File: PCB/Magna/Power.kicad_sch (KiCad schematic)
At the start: 40 parts, among them U901 TPS61040DBV, U902 XL1509-ADJ, U903 WS3222D, U904 AMS1117-5.0, U905 AP2171W

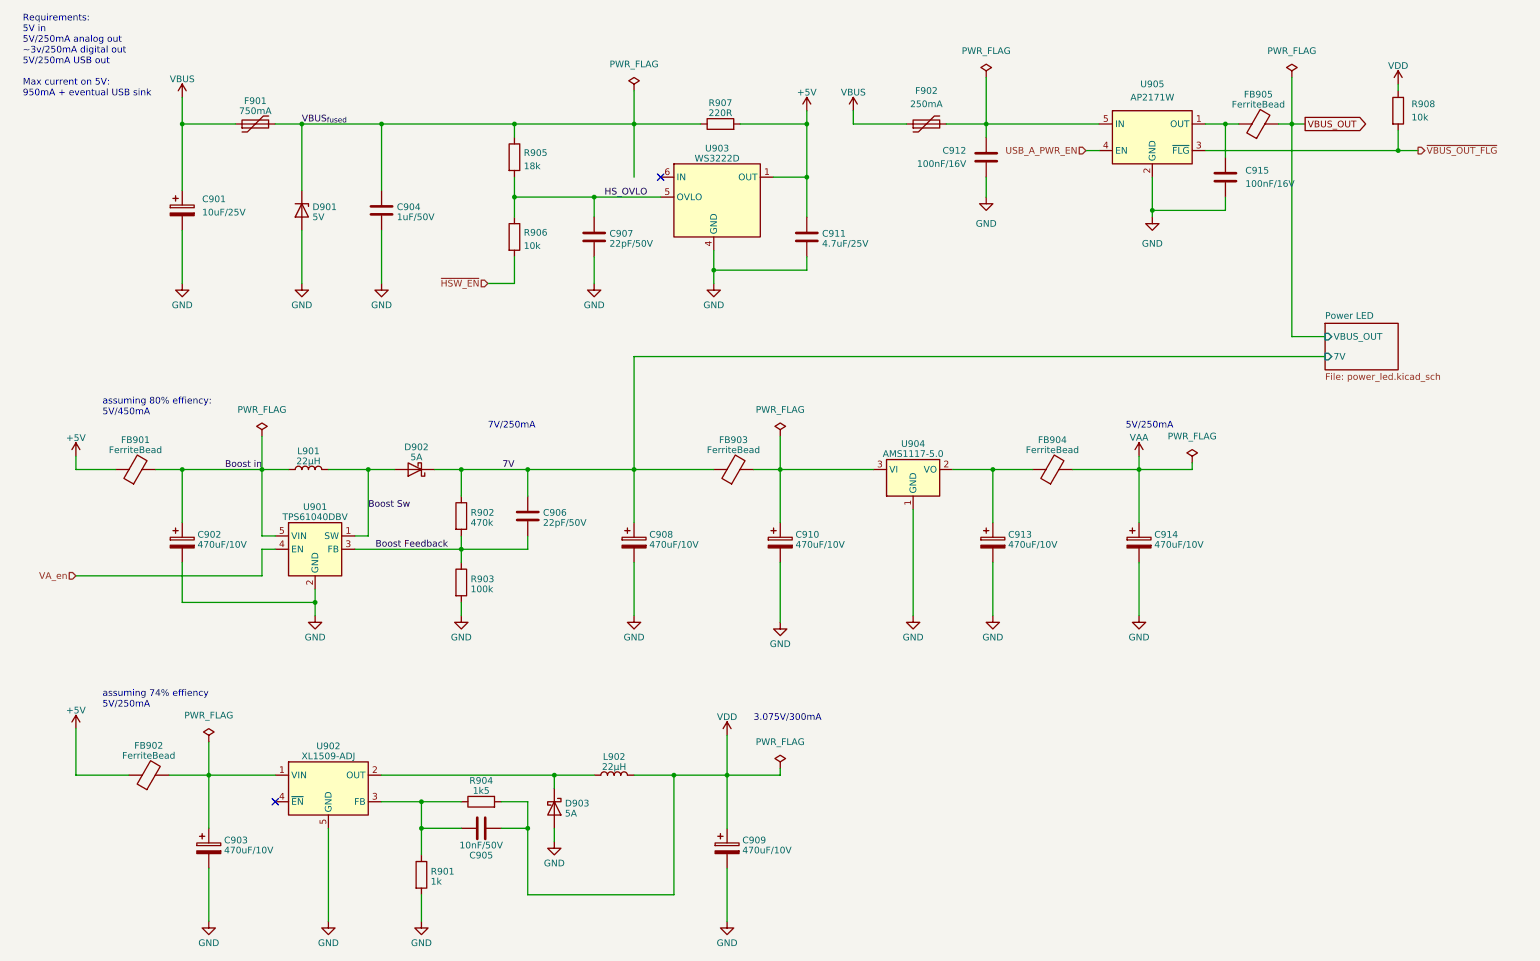
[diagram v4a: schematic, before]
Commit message: Select parts for all components
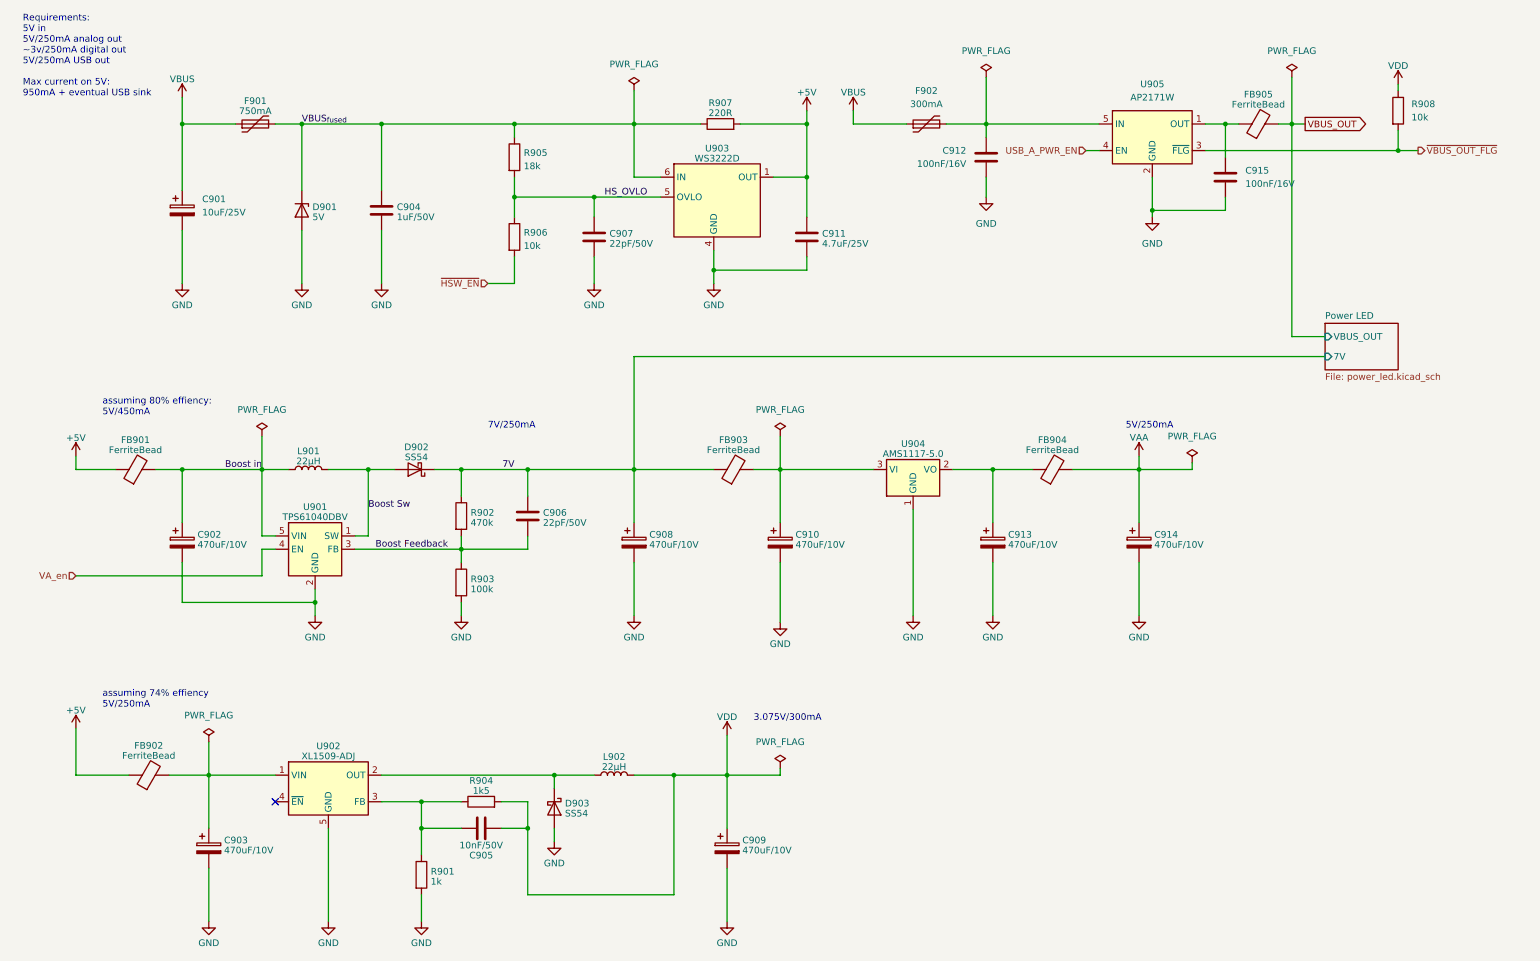
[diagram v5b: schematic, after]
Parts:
- D901: footprint Diode_SMD:D_SMC -> Diode_SMD:D_MELF_Handsoldering; LCSC (none) -> C8062
- D902, D903: value 5A -> SS54; footprint Diode_SMD:D_SMA -> Diode_SMD:D_SMA_Handsoldering; LCSC (none) -> C22452
- F901: footprint Fuse:Fuse_0805_2012Metric -> Fuse:Fuse_2920_7451Metric_Pad2.10x5.45mm_HandSolder; LCSC (none) -> C20822
- F902: value 250mA -> 300mA; footprint (none) -> Fuse:Fuse_2920_7451Metric_Pad2.10x5.45mm_HandSolder; LCSC (none) -> C20820
- FB901, FB902, FB904, FB905: LCSC C1002 -> C1015
- FB903: LCSC C1017 -> C1015
- R901: footprint Resistor_SMD:R_0402_1005Metric -> Resistor_SMD:R_0805_2012Metric_Pad1.20x1.40mm_HandSolder; LCSC (none) -> C17513
- R902: footprint Resistor_SMD:R_0402_1005Metric -> Resistor_SMD:R_0805_2012Metric_Pad1.20x1.40mm_HandSolder; LCSC (none) -> C17709
- R903: footprint Resistor_SMD:R_0402_1005Metric -> Resistor_SMD:R_0805_2012Metric_Pad1.20x1.40mm_HandSolder; LCSC (none) -> C149504
- R904: footprint Resistor_SMD:R_0402_1005Metric -> Resistor_SMD:R_0805_2012Metric_Pad1.20x1.40mm_HandSolder; LCSC (none) -> C4310
- R905: footprint Resistor_SMD:R_0402_1005Metric -> Resistor_SMD:R_0603_1608Metric_Pad0.98x0.95mm_HandSolder; LCSC (none) -> C25810
- R906: footprint Resistor_SMD:R_0402_1005Metric -> Resistor_SMD:R_0805_2012Metric; LCSC (none) -> C17414
- R907: footprint Resistor_SMD:R_0805_2012Metric -> Resistor_SMD:R_0805_2012Metric_Pad1.20x1.40mm_HandSolder; LCSC (none) -> C17557
- R908: footprint (none) -> Resistor_SMD:R_0805_2012Metric; LCSC (none) -> C17414
- U901: LCSC (none) -> C7722
- U904: LCSC (none) -> C6187
- U905: LCSC (none) -> C110466
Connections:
- net VBUS_{fused} is gone; now on net IN: C904.1, D901.1 (K), F901.2, R905.1, R907.1
- no-connect marks 2 -> 1
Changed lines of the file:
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@@
   )
   (no_connect (at 63.5 165.1))
-  (no_connect (at 137.16 45.72))
   (wire (pts (xy 106.68 170.18) (xy 111.76 170.18))
     (stroke (width 0) (type default))
@@
   )
   (wire (pts (xy 81.28 101.6) (xy 81.28 114.3))
+    (stroke (width 0) (type default))
+  )
+  (wire (pts (xy 132.08 45.72) (xy 137.16 45.72))
     (stroke (width 0) (type default))
   )
@@
     )
     (property "Datasheet" "http://www.advanced-monolithic.com/pdf/ds1117.pdf" (at 187.96 107.95 0)
+      (effects (font (size 1.27 1.27)) hide)
+    )
+    (property "LCSC" "C6187" (at 185.42 101.6 0)
       (effects (font (size 1.27 1.27)) hide)
     )
@@
       (effects (font (size 1.27 1.27)) hide)
     )
-    (property "LCSC" "C1002" (at 39.37 160.02 0)
+    (property "LCSC" "C1015" (at 39.37 160.02 0)
       (effects (font (size 1.27 1.27)) hide)
     )
@@
       (effects (font (size 1.27 1.27)) (justify left))
     )
-    (property "Value" "5A" (at 118.872 167.3298 90)
-      (effects (font (size 1.27 1.27)) (justify left))
-    )
-    (property "Footprint" "Diode_SMD:D_SMA" (at 116.84 166.37 0)
+    (property "Value" "SS54" (at 118.872 167.3298 90)
+      (effects (font (size 1.27 1.27)) (justify left))
+    )
+    (property "Footprint" "Diode_SMD:D_SMA_Handsoldering" (at 116.84 166.37 0)
       (effects (font (size 1.27 1.27)) hide)
     )
@@
       (effects (font (size 1.27 1.27)) hide)
     )
-    (property "LCSC" "" (at 116.84 166.37 0)
+    (property "LCSC" "C22452" (at 116.84 166.37 0)
       (effects (font (size 1.27 1.27)) hide)
     )
@@
     )
     (property "Datasheet" "http://www.ti.com/lit/ds/symlink/tps61040.pdf" (at 66.04 109.22 0)
+      (effects (font (size 1.27 1.27)) hide)
+    )
+    (property "LCSC" "C7722" (at 71.12 116.84 0)
       (effects (font (size 1.27 1.27)) hide)
     )
@@
       (effects (font (size 1.27 1.27)) (justify left))
     )
-    (property "Footprint" "" (at 276.352 33.02 90)
+    (property "Footprint" "Resistor_SMD:R_0805_2012Metric" (at 276.352 33.02 90)
       (effects (font (size 1.27 1.27)) hide)
     )
@@
       (effects (font (size 1.27 1.27)) hide)
     )
+    (property "LCSC" "C17414" (at 278.13 33.02 0)
+      (effects (font (size 1.27 1.27)) hide)
+    )
     (pin "2")
     (pin "1")
@@
       (effects (font (size 1.27 1.27)) (justify left))
     )
-    (property "Footprint" "Resistor_SMD:R_0402_1005Metric" (at 97.282 110.49 90)
+    (property "Footprint" "Resistor_SMD:R_0805_2012Metric_Pad1.20x1.40mm_HandSolder" (at 97.282 110.49 90)
       (effects (font (size 1.27 1.27)) hide)
     )
@@
       (effects (font (size 1.27 1.27)) hide)
     )
-    (property "LCSC" "" (at 99.06 110.49 0)
+    (property "LCSC" "C17709" (at 99.06 110.49 0)
       (effects (font (size 1.27 1.27)) hide)
     )
@@
       (effects (font (size 1.27 1.27)))
     )
-    (property "Footprint" "Resistor_SMD:R_0805_2012Metric" (at 148.59 37.338 90)
+    (property "Footprint" "Resistor_SMD:R_0805_2012Metric_Pad1.20x1.40mm_HandSolder" (at 148.59 37.338 90)
       (effects (font (size 1.27 1.27)) hide)
     )
@@
       (effects (font (size 1.27 1.27)) hide)
     )
-    (property "LCSC" "" (at 148.59 35.56 90)
+    (property "LCSC" "C17557" (at 148.59 35.56 90)
       (effects (font (size 1.27 1.27)) hide)
     )
@@
       (effects (font (size 1.27 1.27)) hide)
     )
-    (property "LCSC" "C1002" (at 212.09 101.6 0)
+    (property "LCSC" "C1015" (at 212.09 101.6 0)
       (effects (font (size 1.27 1.27)) hide)
     )
@@
       (effects (font (size 1.27 1.27)) (justify left))
     )
-    (property "Footprint" "Resistor_SMD:R_0402_1005Metric" (at 97.282 123.19 90)
+    (property "Footprint" "Resistor_SMD:R_0805_2012Metric_Pad1.20x1.40mm_HandSolder" (at 97.282 123.19 90)
       (effects (font (size 1.27 1.27)) hide)
     )
@@
       (effects (font (size 1.27 1.27)) hide)
     )
-    (property "LCSC" "" (at 99.06 123.19 0)
+    (property "LCSC" "C149504" (at 99.06 123.19 0)
       (effects (font (size 1.27 1.27)) hide)
     )
@@
       (effects (font (size 1.27 1.27)) (justify left))
     )
-    (property "Footprint" "Resistor_SMD:R_0402_1005Metric" (at 107.442 41.91 90)
+    (property "Footprint" "Resistor_SMD:R_0603_1608Metric_Pad0.98x0.95mm_HandSolder" (at 107.442 41.91 90)
       (effects (font (size 1.27 1.27)) hide)
     )
@@
       (effects (font (size 1.27 1.27)) hide)
     )
-    (property "LCSC" "" (at 109.22 41.91 0)
+    (property "LCSC" "C25810" (at 109.22 41.91 0)
       (effects (font (size 1.27 1.27)) hide)
     )
@@
       (effects (font (size 1.27 1.27)))
     )
-    (property "Value" "5A" (at 90.4875 99.2411 0)
-      (effects (font (size 1.27 1.27)))
-    )
-    (property "Footprint" "Diode_SMD:D_SMA" (at 90.17 101.6 0)
+    (property "Value" "SS54" (at 90.4875 99.2411 0)
+      (effects (font (size 1.27 1.27)))
+    )
+    (property "Footprint" "Diode_SMD:D_SMA_Handsoldering" (at 90.17 101.6 0)
       (effects (font (size 1.27 1.27)) hide)
     )
@@
       (effects (font (size 1.27 1.27)) hide)
     )
-    (property "LCSC" "" (at 90.17 101.6 0)
+    (property "LCSC" "C22452" (at 90.17 101.6 0)
       (effects (font (size 1.27 1.27)) hide)
     )
@@
       (effects (font (size 1.27 1.27)) (justify left))
     )
-    (property "Footprint" "Resistor_SMD:R_0402_1005Metric" (at 89.662 179.07 90)
+    (property "Footprint" "Resistor_SMD:R_0805_2012Metric_Pad1.20x1.40mm_HandSolder" (at 89.662 179.07 90)
       (effects (font (size 1.27 1.27)) hide)
     )
@@
       (effects (font (size 1.27 1.27)) hide)
     )
-    (property "LCSC" "" (at 91.44 179.07 0)
+    (property "LCSC" "C17513" (at 91.44 179.07 0)
       (effects (font (size 1.27 1.27)) hide)
     )
@@
     )
     (property "Datasheet" "https://www.diodes.com/assets/Datasheets/AP2161.pdf" (at 231.14 36.83 0)
+      (effects (font (size 1.27 1.27)) hide)
+    )
+    (property "LCSC" "C110466" (at 231.14 38.1 0)
       (effects (font (size 1.27 1.27)) hide)
     )
@@
       (effects (font (size 1.27 1.27)) (justify left))
     )
-    (property "Footprint" "Resistor_SMD:R_0402_1005Metric" (at 107.442 57.15 90)
+    (property "Footprint" "Resistor_SMD:R_0805_2012Metric" (at 107.442 57.15 90)
       (effects (font (size 1.27 1.27)) hide)
     )
@@
       (effects (font (size 1.27 1.27)) hide)
     )
-    (property "LCSC" "" (at 109.22 57.15 0)
+    (property "LCSC" "C17414" (at 109.22 57.15 0)
       (effects (font (size 1.27 1.27)) hide)
     )
@@
       (effects (font (size 1.27 1.27)) (justify left))
     )
-    (property "Footprint" "Diode_SMD:D_SMC" (at 68.58 52.07 0)
+    (property "Footprint" "Diode_SMD:D_MELF_Handsoldering" (at 68.58 52.07 0)
       (effects (font (size 1.27 1.27)) hide)
     )
@@
       (effects (font (size 1.27 1.27)) hide)
     )
-    (property "LCSC" "" (at 68.58 52.07 90)
+    (property "LCSC" "C8062" (at 68.58 52.07 90)
       (effects (font (size 1.27 1.27)) hide)
     )
@@
       (effects (font (size 1.27 1.27)))
     )
-    (property "Value" "250mA" (at 187.96 31.75 90)
-      (effects (font (size 1.27 1.27)))
-    )
-    (property "Footprint" "" (at 193.04 34.29 0)
+    (property "Value" "300mA" (at 187.96 31.75 90)
+      (effects (font (size 1.27 1.27)))
+    )
+    (property "Footprint" "Fuse:Fuse_2920_7451Metric_Pad2.10x5.45mm_HandSolder" (at 193.04 34.29 0)
       (effects (font (size 1.27 1.27)) (justify left) hide)
     )
@@
       (effects (font (size 1.27 1.27)) hide)
     )
+    (property "LCSC" "C20820" (at 187.96 35.56 0)
+      (effects (font (size 1.27 1.27)) hide)
+    )
     (pin "2")
     (pin "1")
@@
       (effects (font (size 1.27 1.27)) hide)
     )
-    (property "LCSC" "C1017" (at 151.13 101.6 0)
+    (property "LCSC" "C1015" (at 151.13 101.6 0)
       (effects (font (size 1.27 1.27)) hide)
     )
@@
       (effects (font (size 1.27 1.27)))
     )
-    (property "Footprint" "Resistor_SMD:R_0402_1005Metric" (at 102.87 166.878 90)
+    (property "Footprint" "Resistor_SMD:R_0805_2012Metric_Pad1.20x1.40mm_HandSolder" (at 102.87 166.878 90)
       (effects (font (size 1.27 1.27)) hide)
     )
@@
       (effects (font (size 1.27 1.27)) hide)
     )
-    (property "LCSC" "" (at 102.87 165.1 90)
+    (property "LCSC" "C4310" (at 102.87 165.1 90)
       (effects (font (size 1.27 1.27)) hide)
     )
@@
       (effects (font (size 1.27 1.27)) hide)
     )
-    (property "LCSC" "C1002" (at 251.46 35.56 0)
+    (property "LCSC" "C1015" (at 251.46 35.56 0)
       (effects (font (size 1.27 1.27)) hide)
     )
@@
       (effects (font (size 1.27 1.27)) hide)
     )
-    (property "LCSC" "C1002" (at 36.83 101.6 0)
+    (property "LCSC" "C1015" (at 36.83 101.6 0)
       (effects (font (size 1.27 1.27)) hide)
     )
@@
       (effects (font (size 1.27 1.27)))
     )
-    (property "Footprint" "Fuse:Fuse_0805_2012Metric" (at 64.77 34.29 0)
+    (property "Footprint" "Fuse:Fuse_2920_7451Metric_Pad2.10x5.45mm_HandSolder" (at 64.77 34.29 0)
       (effects (font (size 1.27 1.27)) (justify left) hide)
     )
@@
       (effects (font (size 1.27 1.27)) hide)
     )
+    (property "LCSC" "C20822" (at 59.69 35.56 0)
+      (effects (font (size 1.27 1.27)) hide)
+    )

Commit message: Add even more component footprints and partnumbers
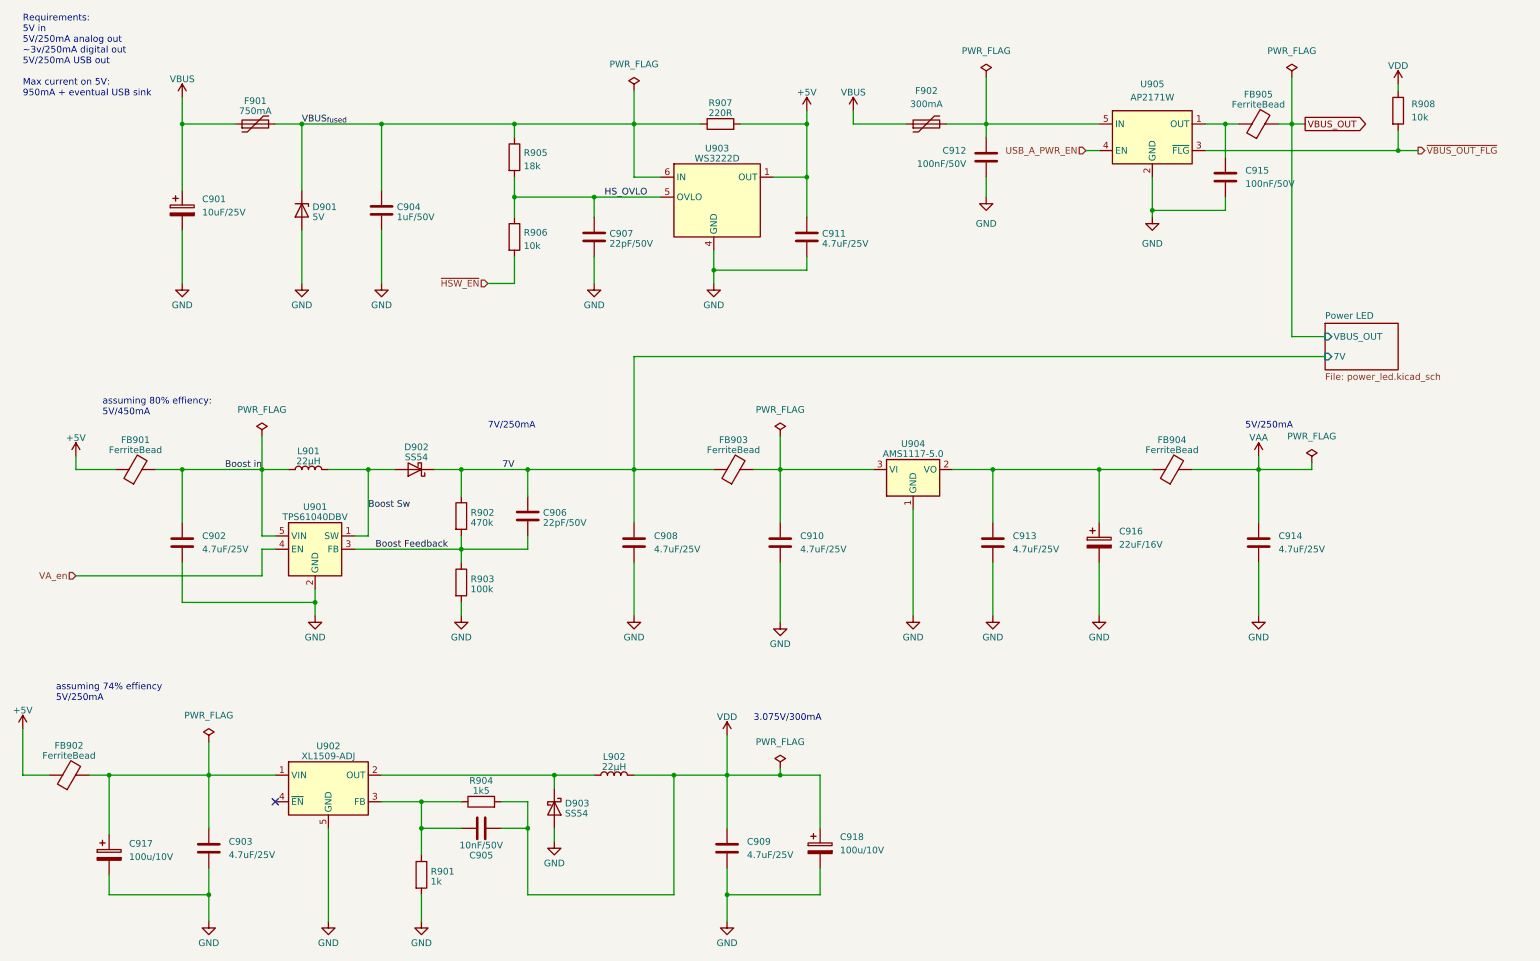
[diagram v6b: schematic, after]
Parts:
- added C916: 22uF/16V, Capacitor_SMD:CP_Elec_5x5.8, symbol Device:C_Polarized
- added C917, C918: 100u/10V, Capacitor_SMD:CP_Elec_6.3x5.8, symbol Device:C_Polarized
- C902, C903, C908, C909, C910, C913, C914: value 470uF/10V -> 4.7uF/25V; footprint Capacitor_SMD:CP_Elec_6.3x7.7 -> Capacitor_SMD:C_0805_2012Metric_Pad1.18x1.45mm_HandSolder; symbol Device:C_Polarized -> Device:C; LCSC C2163263 -> C1779
- C904, C905, C906, C907, C911: footprint Capacitor_SMD:C_0805_2012Metric -> Capacitor_SMD:C_0805_2012Metric_Pad1.18x1.45mm_HandSolder
- C912, C915: value 100nF/16V -> 100nF/50V; footprint Capacitor_SMD:C_0805_2012Metric -> Capacitor_SMD:C_0805_2012Metric_Pad1.18x1.45mm_HandSolder; LCSC C218638 -> C49678
- L901, L902: footprint SkrooterFootprints:MSCD43 -> Skrooter_footprints:MSCD43
- R906, R908: footprint Resistor_SMD:R_0805_2012Metric -> Resistor_SMD:R_0805_2012Metric_Pad1.20x1.40mm_HandSolder
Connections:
- net GND: now also C916.2, C917.2, C918.2
- net VDD: now also C918.1
- net at C913.1, FB904.1, U904.2 (VO): now also C916.1
- net at C903.1, FB902.2, U902.1 (VIN): now also C917.1
- net IN renamed VBUS_{fused}
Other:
- moved on the sheet: FB902, FB904
